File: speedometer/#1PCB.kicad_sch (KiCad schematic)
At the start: 70 parts, among them J1 Conn_01x02, J2 CAN to outer connector, J3 DTF13-6P, U1 A1104xLH, U2 NE555P, U3 A1104xLH, U4 NE555P, U5 A1104xLH, U6 NE555P, U7 MCP2515-I, U8 TJA1050DRG, X1 ${ALTIUM_VALUE}

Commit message: aw hell naw
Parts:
- removed J1: Conn_01x02, Connector_Wire:SolderWire-0.75sqmm_1x02_P4.8mm_D1.25mm_OD2.3mm, symbol Connector_Generic:Conn_01x02
- removed J2: CAN to outer connector, Connector_Wire:SolderWire-0.1sqmm_1x04_P3.6mm_D0.4mm_OD1mm, symbol Connector_Generic:Conn_01x04
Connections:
- net INT: now reaches A1.5 (D2)
- no-connect marks 28 -> 26

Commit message: Add F points
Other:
- moved on the sheet: J3
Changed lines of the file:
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@@
 	(global_label "GND"
 		(shape input)
-		(at 356.87 184.15 180)
+		(at 229.87 227.33 180)
 		(fields_autoplaced yes)
 		(effects
@@
 		)
 		(property "Intersheetrefs" "${INTERSHEET_REFS}"
-			(at 350.0143 184.15 0)
+			(at 223.0143 227.33 0)
 			(effects
 				(font
@@
 	(global_label "Low"
 		(shape input)
-		(at 356.87 191.77 180)
+		(at 229.87 234.95 180)
 		(fields_autoplaced yes)
 		(effects
@@
 		)
 		(property "Intersheetrefs" "${INTERSHEET_REFS}"
-			(at 350.3772 191.77 0)
+			(at 223.3772 234.95 0)
 			(effects
 				(font
@@
 	(global_label "High"
 		(shape input)
-		(at 356.87 189.23 180)
+		(at 229.87 232.41 180)
 		(fields_autoplaced yes)
 		(effects
@@
 		)
 		(property "Intersheetrefs" "${INTERSHEET_REFS}"
-			(at 349.6515 189.23 0)
+			(at 222.6515 232.41 0)
 			(effects
 				(font
@@
 	(global_label "High"
 		(shape input)
-		(at 356.87 194.31 180)
+		(at 229.87 237.49 180)
 		(fields_autoplaced yes)
 		(effects
@@
 		)
 		(property "Intersheetrefs" "${INTERSHEET_REFS}"
-			(at 349.6515 194.31 0)
+			(at 222.6515 237.49 0)
 			(effects
 				(font
@@
 	(global_label "Low"
 		(shape input)
-		(at 356.87 186.69 180)
+		(at 229.87 229.87 180)
 		(fields_autoplaced yes)
 		(effects
@@
 		)
 		(property "Intersheetrefs" "${INTERSHEET_REFS}"
-			(at 350.3772 186.69 0)
+			(at 223.3772 229.87 0)
 			(effects
 				(font
@@
 	(global_label "+5V"
 		(shape input)
-		(at 356.87 181.61 180)
+		(at 229.87 224.79 180)
 		(fields_autoplaced yes)
 		(effects
@@
 		)
 		(property "Intersheetrefs" "${INTERSHEET_REFS}"
-			(at 350.0143 181.61 0)
+			(at 223.0143 224.79 0)
 			(effects
 				(font
@@
 	(symbol
 		(lib_id "DTF13-6P:DTF13-6P")
-		(at 367.03 186.69 0)
+		(at 240.03 229.87 0)
 		(unit 1)
 		(exclude_from_sim no)
@@
 		(dnp no)
 		(property "Reference" "J3"
-			(at 363.728 198.12 0)
+			(at 236.728 241.3 0)
 			(effects
 				(font
@@
 		)
 		(property "Value" "DTF13-6P"
-			(at 363.728 200.66 0)
+			(at 236.728 243.84 0)
 			(effects
 				(font
@@
 		)
 		(property "Footprint" "New Tachometer-2025-12-06_105253:TE_DTF13-6P"
-			(at 367.03 186.69 0)
+			(at 240.03 229.87 0)
 			(effects
 				(font
@@
 		)
 		(property "Datasheet" ""
-			(at 367.03 186.69 0)
+			(at 240.03 229.87 0)
 			(effects
 				(font
@@
 		)
 		(property "Description" ""
-			(at 367.03 186.69 0)
+			(at 240.03 229.87 0)
 			(effects
 				(font
@@
 		)
 		(property "Comment" "DTF13-6P"
-			(at 367.03 186.69 0)
+			(at 240.03 229.87 0)
 			(effects
 				(font
@@
 		)
 		(property "MF" "TE Connectivity"
-			(at 367.03 186.69 0)
+			(at 240.03 229.87 0)
 			(effects
 				(font
@@
 		)
 		(property "MAXIMUM_PACKAGE_HEIGHT" "22.35mm"
-			(at 367.03 186.69 0)
+			(at 240.03 229.87 0)
 			(effects
 				(font
@@
 		)
 		(property "Package" "None"
-			(at 367.03 186.69 0)
+			(at 240.03 229.87 0)
 			(effects
 				(font
@@
 		)
 		(property "Price" "None"
-			(at 367.03 186.69 0)
+			(at 240.03 229.87 0)
 			(effects
 				(font
@@
 		)
 		(property "Check_prices" "https://www.snapeda.com/parts/DTF13-6P/TE+Connectivity+Deutsch+Connectors/view-part/?ref=eda"
-			(at 367.03 186.69 0)
+			(at 240.03 229.87 0)
 			(effects
 				(font
@@
 		)
 		(property "STANDARD" "Manufacturer Recommendations"
-			(at 367.03 186.69 0)
+			(at 240.03 229.87 0)
 			(effects
 				(font
@@
 		)
 		(property "PARTREV" "B"
-			(at 367.03 186.69 0)
+			(at 240.03 229.87 0)
 			(effects
 				(font
@@
 		)
 		(property "SnapEDA_Link" "https://www.snapeda.com/parts/DTF13-6P/TE+Connectivity+Deutsch+Connectors/view-part/?ref=snap"
-			(at 367.03 186.69 0)
+			(at 240.03 229.87 0)
 			(effects
 				(font
@@
 		)
 		(property "MP" "DTF13-6P"
-			(at 367.03 186.69 0)
+			(at 240.03 229.87 0)
 			(effects
 				(font
@@
 		)
 		(property "EU_RoHS_Compliance" "Compliant with Exemptions"
-			(at 367.03 186.69 0)
+			(at 240.03 229.87 0)
 			(effects
 				(font
@@
 		)
 		(property "Description_1" "Connector, 6-Way, Black, Polyamide, DT Series | TE Connectivity DTF13-6P"
-			(at 367.03 186.69 0)
+			(at 240.03 229.87 0)
 			(effects
 				(font
@@
 		)
 		(property "Availability" "In Stock"
-			(at 367.03 186.69 0)
+			(at 240.03 229.87 0)
 			(effects
 				(font
@@
 		)
 		(property "MANUFACTURER" "TE Connectivity"
-			(at 367.03 186.69 0)
+			(at 240.03 229.87 0)
 			(effects
 				(font

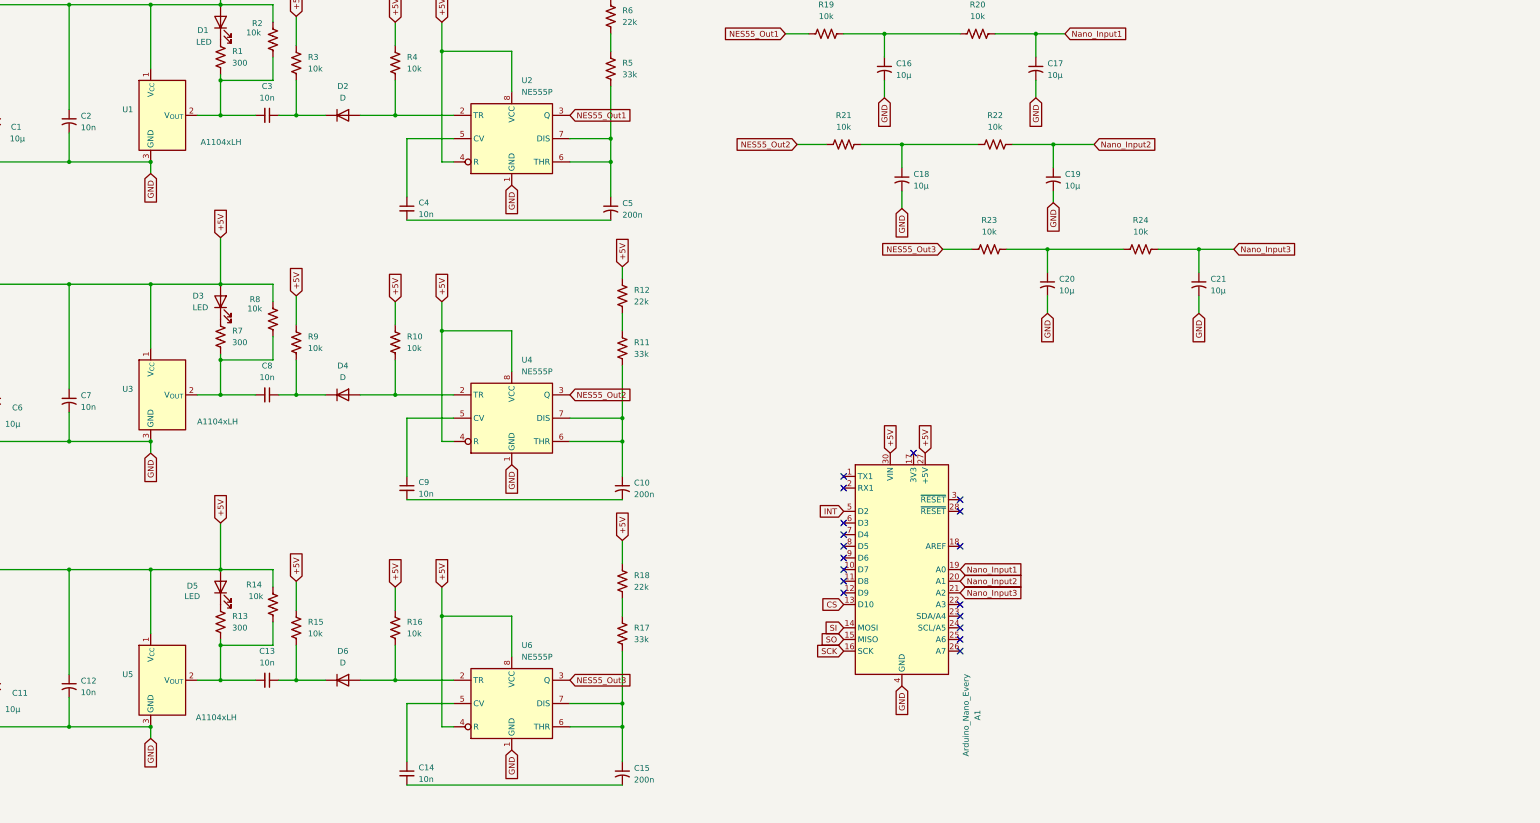
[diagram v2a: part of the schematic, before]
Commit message: Fixed the speedometer silly
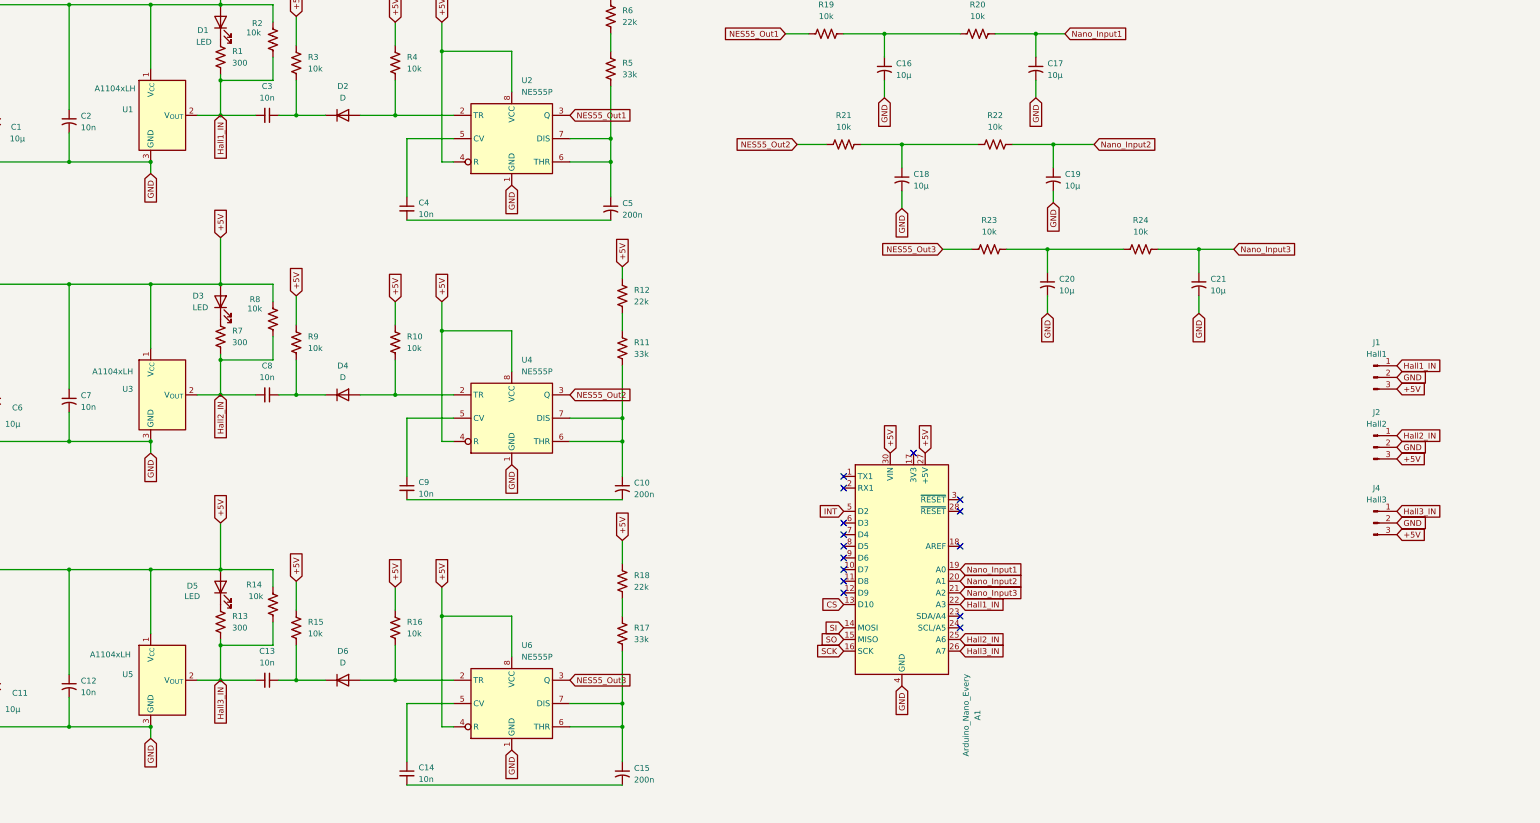
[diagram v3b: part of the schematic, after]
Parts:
- added J1: Hall1, Connector_PinHeader_2.54mm:PinHeader_1x03_P2.54mm_Vertical, symbol Connector:Conn_01x03_Pin
- added J2: Hall2, Connector_PinHeader_2.54mm:PinHeader_1x03_P2.54mm_Vertical, symbol Connector:Conn_01x03_Pin
- added J4: Hall3, Connector_PinHeader_2.54mm:PinHeader_1x03_P2.54mm_Vertical, symbol Connector:Conn_01x03_Pin
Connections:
- net GND: now also J1.2 (Pin_2), J2.2 (Pin_2), J4.2 (Pin_2)
- net VCC: now also J1.3 (Pin_3), J2.3 (Pin_3), J4.3 (Pin_3)
- net Hall2_IN: now reaches C8.2, R7.2, R8.2, U3.2 (V_{OUT})
- net Hall2_IN: now also A1.25 (A6), J2.1 (Pin_1)
- net Hall1_IN: now reaches C3.2, R1.2, R2.2, U1.2 (V_{OUT})
- net Hall1_IN: now also A1.22 (A3), J1.1 (Pin_1)
- net Hall3_IN: now reaches C13.2, R13.2, R14.2, U5.2 (V_{OUT})
- net Hall3_IN: now also A1.26 (A7), J4.1 (Pin_1)
- no-connect marks 26 -> 23
